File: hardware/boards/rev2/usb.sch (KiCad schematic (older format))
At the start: 35 parts, among them J2 USB_B_Micro, U8 93LCxxBxxOT, U9 FT2232H, Y1 12MHz

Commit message: reorganize schematic
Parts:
- U9: symbol Interface_USB:FT2232H -> fmcw-rescue:FT2232H-Interface_USB
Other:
- note added: "150 mA"
- note added: "70 mA"

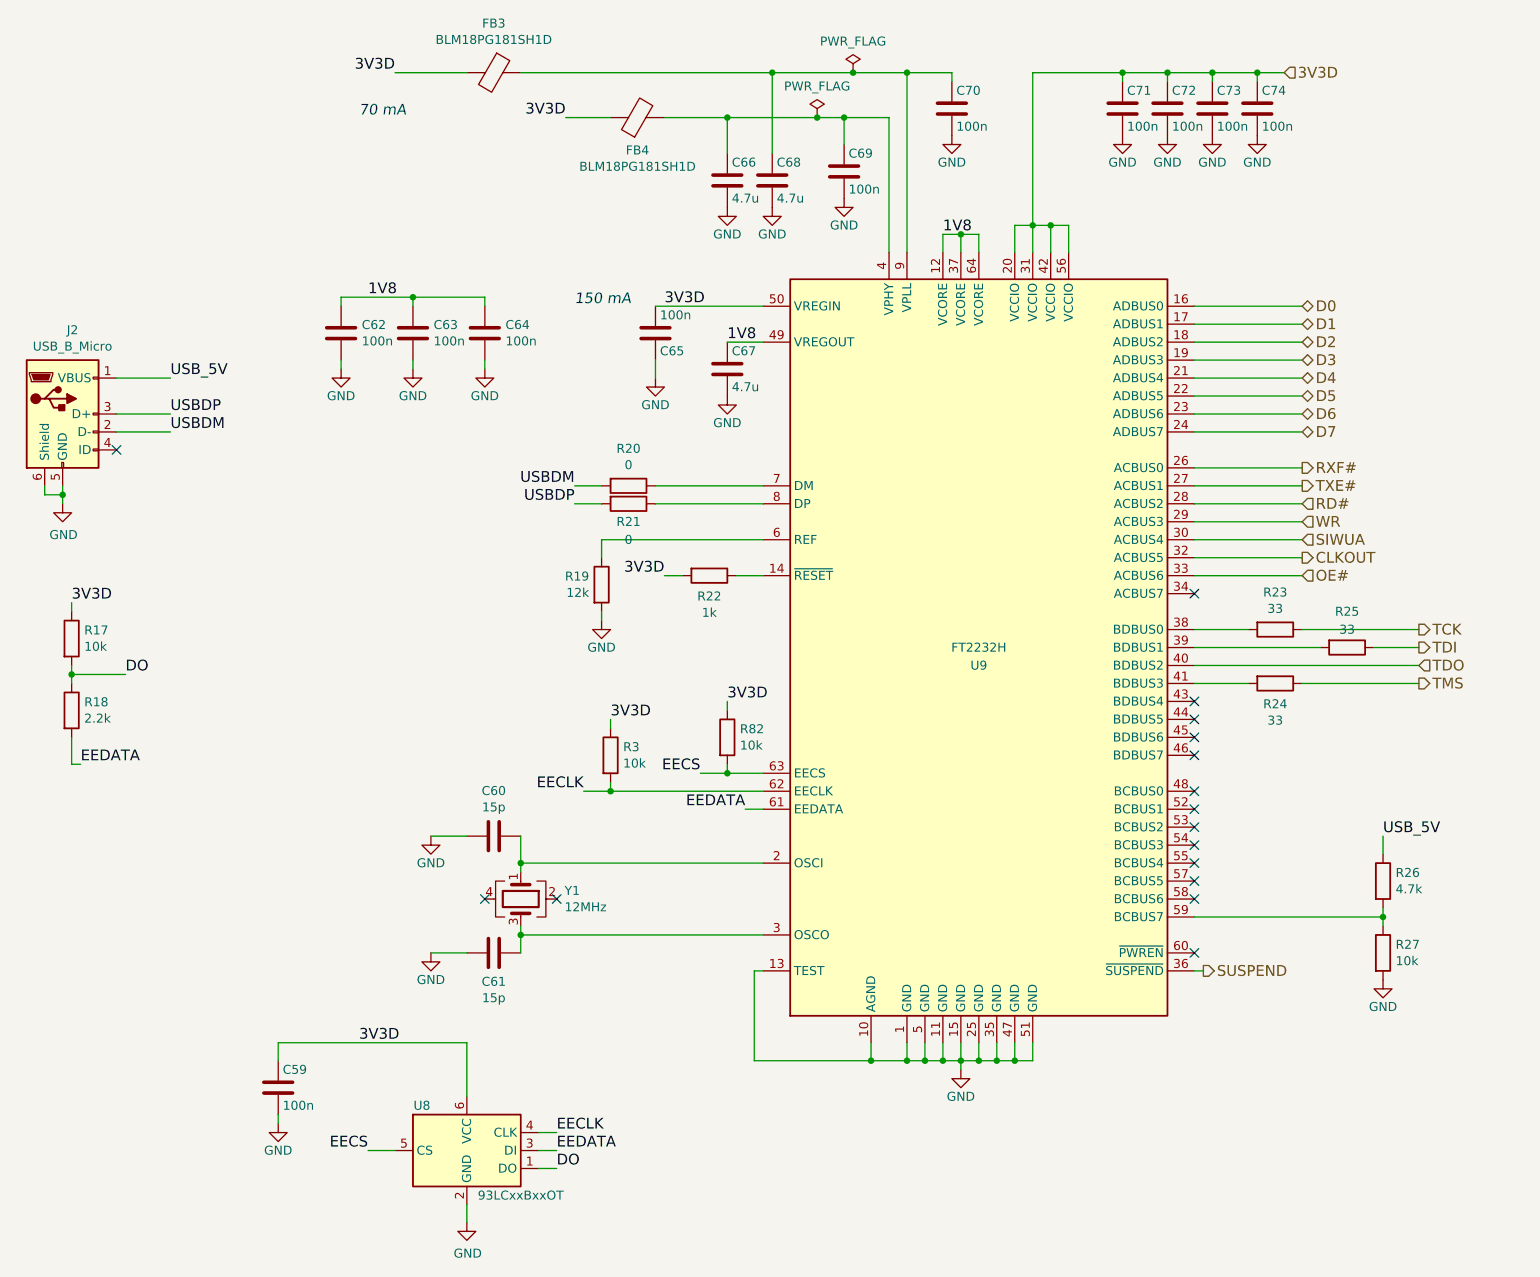
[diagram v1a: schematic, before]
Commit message: revert to kicad v5 for pcb gen
V6 contains a few bugs and a V6 board cannot be edited with V5.
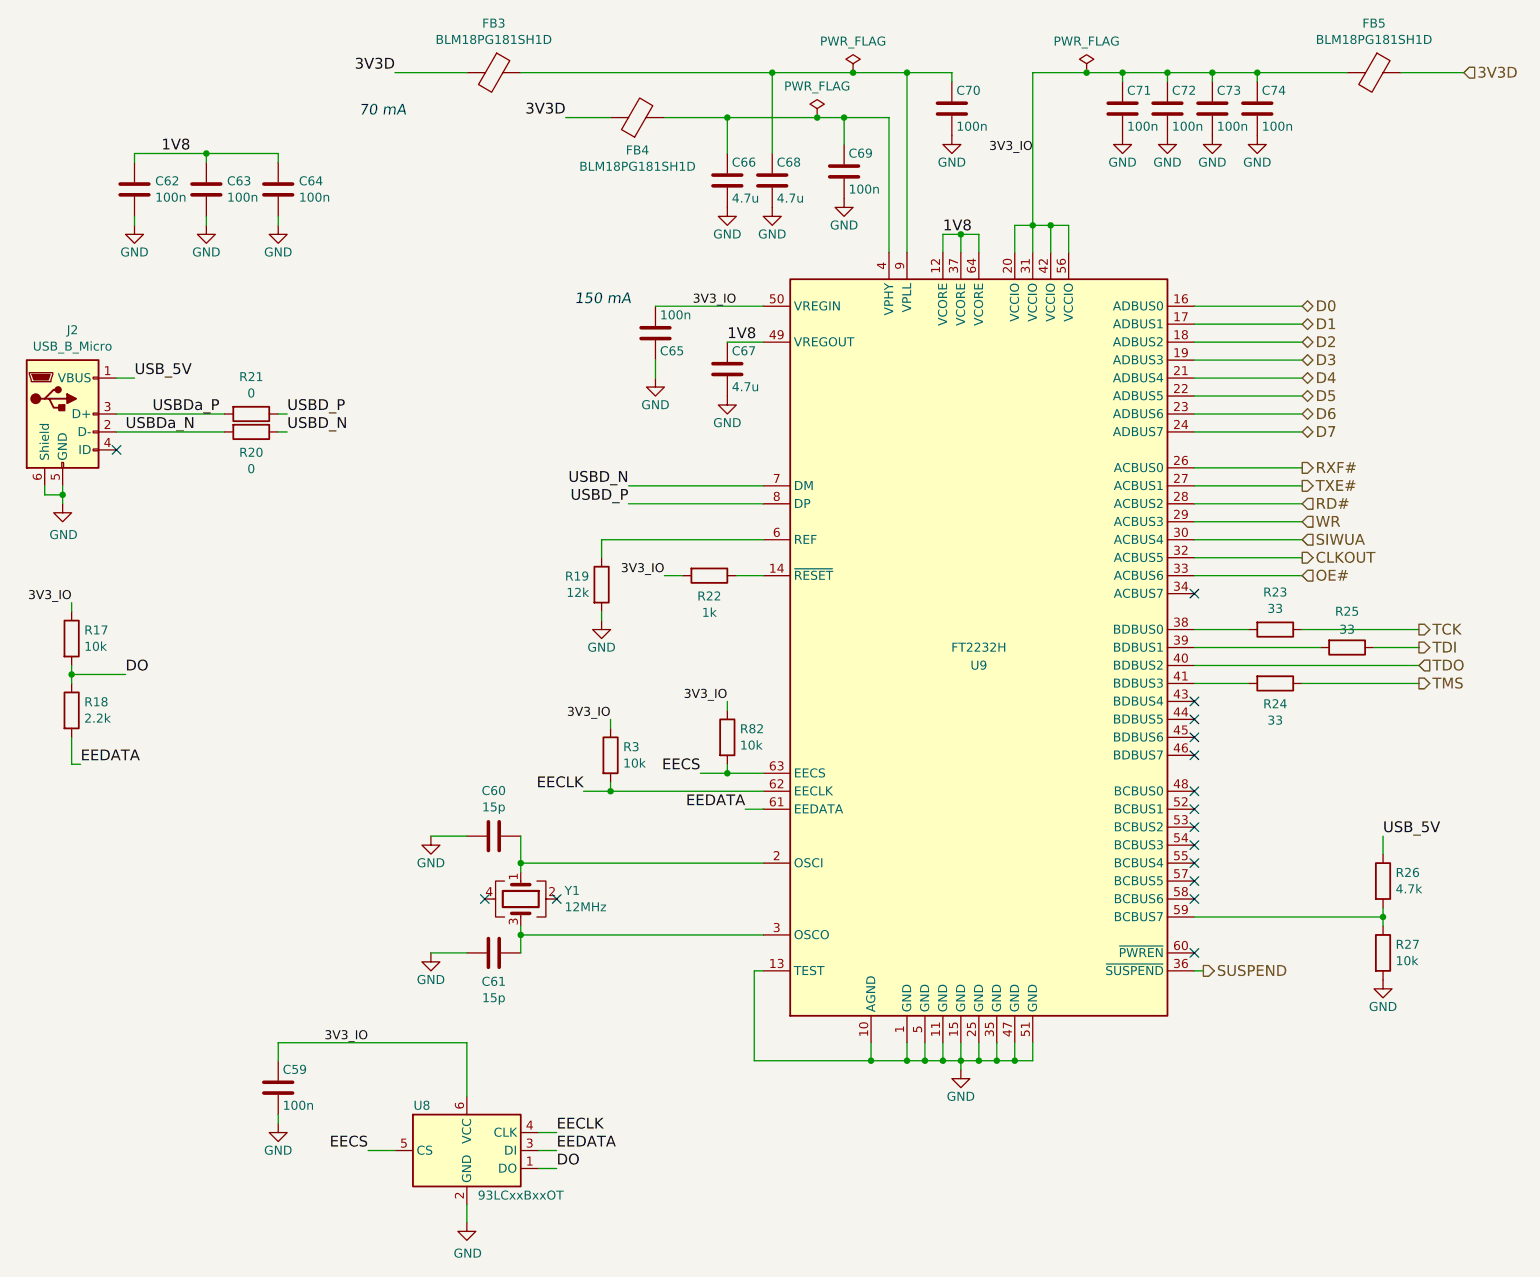
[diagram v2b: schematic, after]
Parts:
- added FB5: BLM18PG181SH1D, Inductor_SMD:L_0603_1608Metric, symbol Device:Ferrite_Bead
- Y1: footprint fmcw:ABM10 -> Crystal:Crystal_SMD_Abracon_ABM10-4Pin_2.5x2.0mm
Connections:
- net 3V3D: now also FB5.1; no longer C59.1, C65.2, C71.1, C72.1, C73.1, C74.1, R17.1, R22.2, R3.1, R82.1, U8.6 (VCC), U9.20 (VCCIO), U9.31 (VCCIO), U9.42 (VCCIO), U9.50 (VREGIN), U9.56 (VCCIO)
- net USBD_N: now reaches R20.1, U9.7 (DM)
- net USBD_P: now reaches R21.1, U9.8 (DP)
- net USBDM renamed USBDa_N
- net USBDP renamed USBDa_P
- new net 3V3_IO: C59.1, C65.2, C71.1, C72.1, C73.1, C74.1, FB5.2, R17.1, R22.2, R3.1, R82.1, U8.6 (VCC), U9.20 (VCCIO), U9.31 (VCCIO), U9.42 (VCCIO), U9.50 (VREGIN), U9.56 (VCCIO)
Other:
- moved on the sheet: C62, C63, C64, R20, R21
